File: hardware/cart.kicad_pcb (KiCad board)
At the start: 2 copper layers, 83.8 x 38.3 mm, 4 parts, among them P1 MD-CART-FINGERS

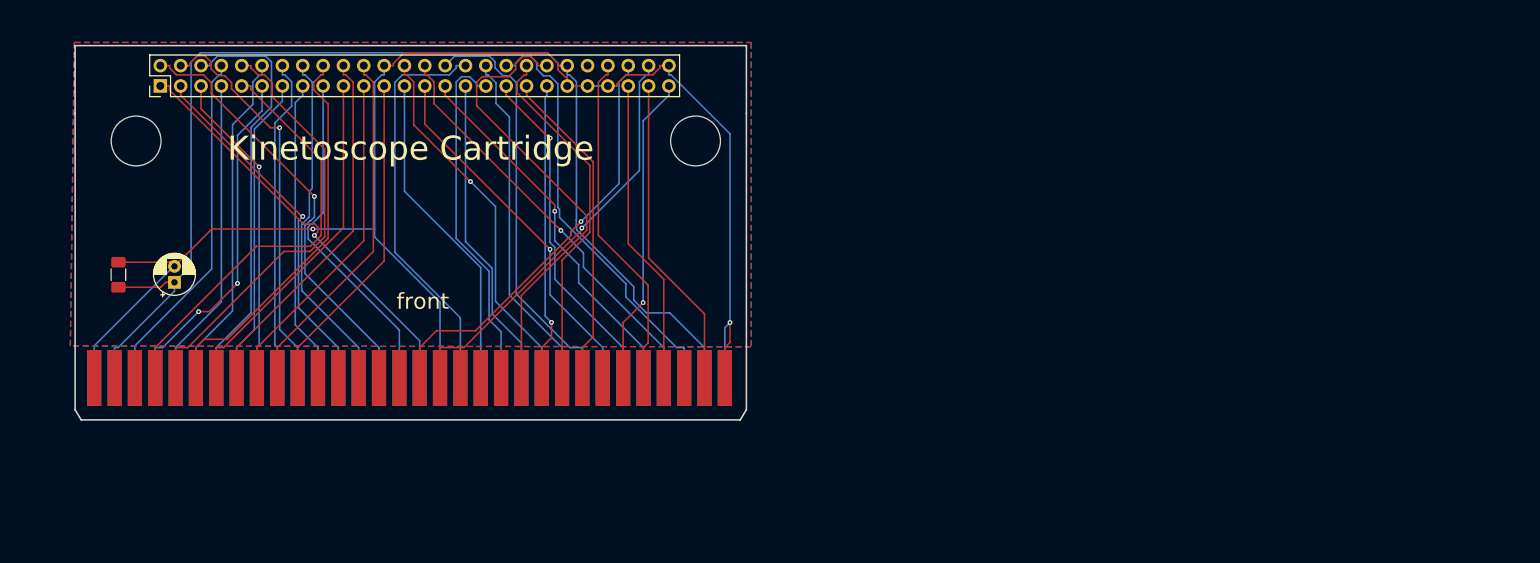
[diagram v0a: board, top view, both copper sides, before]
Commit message: Massively reorganize board designs
Now planning to have most assembly done by JLCPCB, so trace sizes,
part selections, etc. are set accordingly.

New boards are:
 - cartridge interface & flash
 - microcontroller & registers
 - sram x2
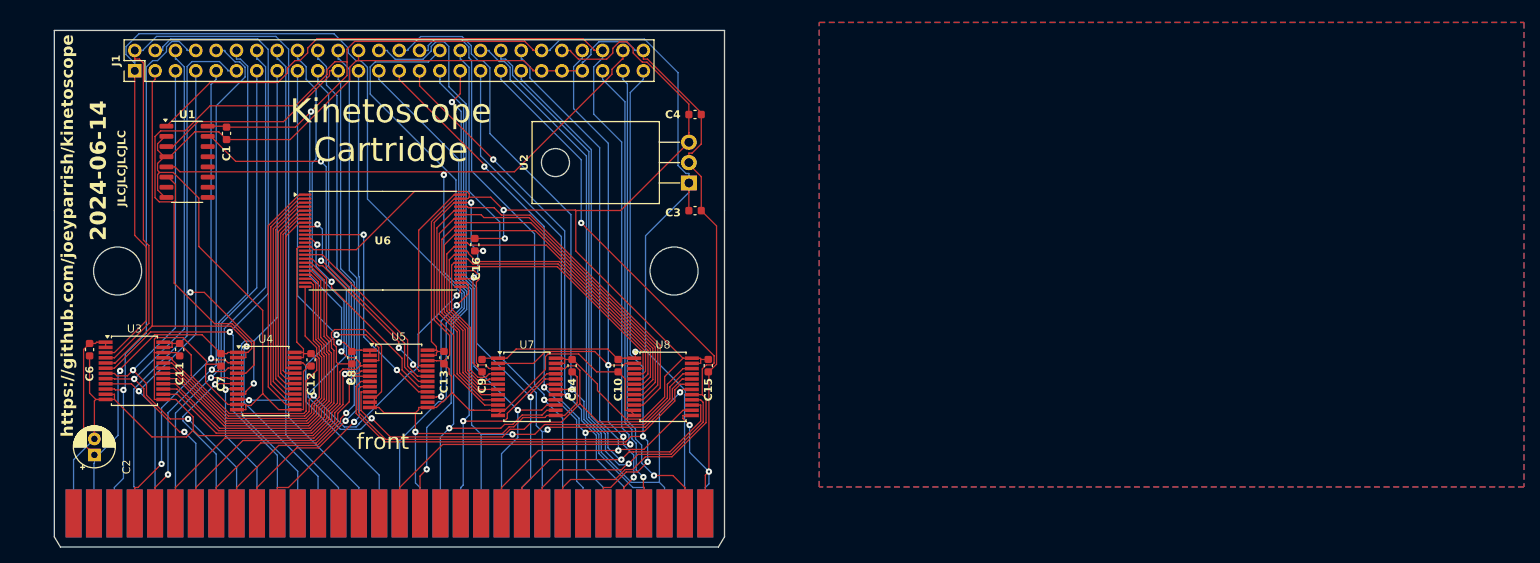
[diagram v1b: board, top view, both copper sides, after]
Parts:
- added C10: 22nF, Capacitor_SMD:C_0603_1608Metric, F.Cu at (83.4, 55.4)
- added C11: 22nF, Capacitor_SMD:C_0603_1608Metric, F.Cu at (28.6, 53.4)
- added C12: 22nF, Capacitor_SMD:C_0603_1608Metric, F.Cu at (45.0, 54.6)
- added C13: 22nF, Capacitor_SMD:C_0603_1608Metric, F.Cu at (61.6, 54.4)
- added C14: 22nF, Capacitor_SMD:C_0603_1608Metric, F.Cu at (77.7, 55.4)
- added C15: 22nF, Capacitor_SMD:C_0603_1608Metric, F.Cu at (94.7, 55.4)
- added C16: 22nF, Capacitor_SMD:C_0603_1608Metric, F.Cu at (65.5, 40.2)
- added C3: 4.7uF, Capacitor_SMD:C_0603_1608Metric, F.Cu at (93.0, 36.0)
- added C4: 1uF, Capacitor_SMD:C_0603_1608Metric, F.Cu at (93.0, 24.0)
- added C6: 22nF, Capacitor_SMD:C_0603_1608Metric, F.Cu at (17.4, 53.4)
- added C7: 22nF, Capacitor_SMD:C_0603_1608Metric, F.Cu at (33.8, 54.6)
- added C8: 22nF, Capacitor_SMD:C_0603_1608Metric, F.Cu at (50.1, 54.4)
- added C9: 22nF, Capacitor_SMD:C_0603_1608Metric, F.Cu at (66.4, 55.4)
- added U1: decoder, Package_SO:SO-16_3.9x9.9mm_P1.27mm, F.Cu at (29.6, 29.9)
- added U2: 1.5A @ 3.3V, Package_TO_SOT_THT:TO-220-3_Horizontal_TabDown, F.Cu at (92.2, 32.5)
- added U3: 3.3V <=> 5V, Package_SO:SSOP-24_5.3x8.2mm_P0.65mm, F.Cu at (23.0, 56.0)
- added U4: 3.3V <=> 5V, Package_SO:SSOP-24_5.3x8.2mm_P0.65mm, F.Cu at (39.4, 57.3)
- added U5: 3.3V <=> 5V, Package_SO:SSOP-24_5.3x8.2mm_P0.65mm, F.Cu at (56.0, 57.0)
- added U6: 1Mx16, Package_SO:TSOP-I-48_18.4x12mm_P0.5mm, F.Cu at (54.0, 39.8)
- added U7: 3.3V <=> 5V, Package_SO:SSOP-24_5.3x8.2mm_P0.65mm, F.Cu at (72.0, 58.0)
- added U8: 3.3V <=> 5V, Package_SO:SSOP-24_5.3x8.2mm_P0.65mm, F.Cu at (89.0, 58.0)
- C1: value 4.7uF -> 22nF; footprint Capacitor_THT:CP_Radial_D5.0mm_P2.00mm -> Capacitor_SMD:C_0603_1608Metric
- C2: value 22nF -> 47uF; footprint Capacitor_SMD:C_1206_3216Metric_Pad1.33x1.80mm_HandSolder -> Capacitor_THT:CP_Radial_D5.0mm_P2.00mm
- J1: footprint kinetoscope-cart-header:kinetoscope-cart-header-half -> Connector_PinHeader_2.54mm:PinHeader_2x26_P2.54mm_Vertical
- P1: value MD-CART-FINGERS -> edge connector
- moved P1 49.1 mm to (13.0, 78.0)
- moved C2 22.7 mm to (18.0, 66.5)
- moved C1 19.7 mm to (34.5, 26.4), turned to -90 degrees
- moved J1 3.72 mm to (23.0, 18.5)
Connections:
- net /5V renamed +5V
- net /GND renamed GND
- J1 pad 44: unconnected-(J1B-3V-Pad44) -> +3.3V
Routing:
- net GND: track 185.7 -> 475.9 mm, vias 2 -> 6
- net +3.3V: track 0.00 -> 222.9 mm, vias 0 -> 2
- net +5V: track 147.2 -> 314.1 mm, vias 0 -> 4
- net /~{FLASH_CE}: track 0.00 -> 118.4 mm, vias 0 -> 2
- net /~{SEGA_CE}: track 52.8 -> 146.2 mm
- net /SEGA_A1: track 51.7 -> 139.1 mm, vias 1 -> 0
- net /~{SEGA_WE_LB}: track 42.5 -> 119.4 mm, vias 0 -> 3
- net /SEGA_A2: track 54.0 -> 124.6 mm, vias 1 -> 0
- net /~{SEGA_RESET}: track 38.8 -> 103.4 mm, vias 1 -> 2
- net /~{SEGA_AS}: track 51.7 -> 110.5 mm, vias 1 -> 2
- net /flash-internal/A0_3V: track 0.00 -> 53.9 mm, vias 0 -> 2
- net /SEGA_A21: track 42.0 -> 90.7 mm, vias 0 -> 1
- net /SEGA_D14: track 37.4 -> 85.9 mm
- net /SEGA_A4: track 49.9 -> 95.3 mm
- net /SEGA_D13: track 44.8 -> 90.2 mm, vias 0 -> 1
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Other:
- board size 83.8 x 38.3 mm -> 83.7 x 42 mm
- board text added: "2024-06-14"
- board text added: "JLCJLCJLCJLC"
- board text added: "This edge beveled, hard-gold plating on these teeth, both sides"
- board text added: "https://github.com/joeyparrish/kinetoscope"
- board text removed: "back"
- board text removed: "front"

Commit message: Redo cart board
The first cartridge board I ordered did not work.  💰🚽

Problems I ran into:
 - The FlashKit Programmer sends 3.3V logic, not 5V logic like the
   Sega
 - I had one hard-coded input to my address decoder inverted
 - One pair of level translators had their supply voltages backward
 - I had hard-coded #OE on the flash chip, but #OE and #WE are
   mutually exclusive on this particular chip

Changes:
 - Add debug connectors (not populated by default) for power and flash
   control signals
 - Fix flash ~OE signal, which is mutually exclusive with ~WE
 - Fix level translators for compatibility with both 3.3V and 5V logic
 - Replace decoder with a smaller, simpler one with no latches and
   5V-tolerance
 - Reorient translators to simplify traces
 - Increase trace width for supply traces
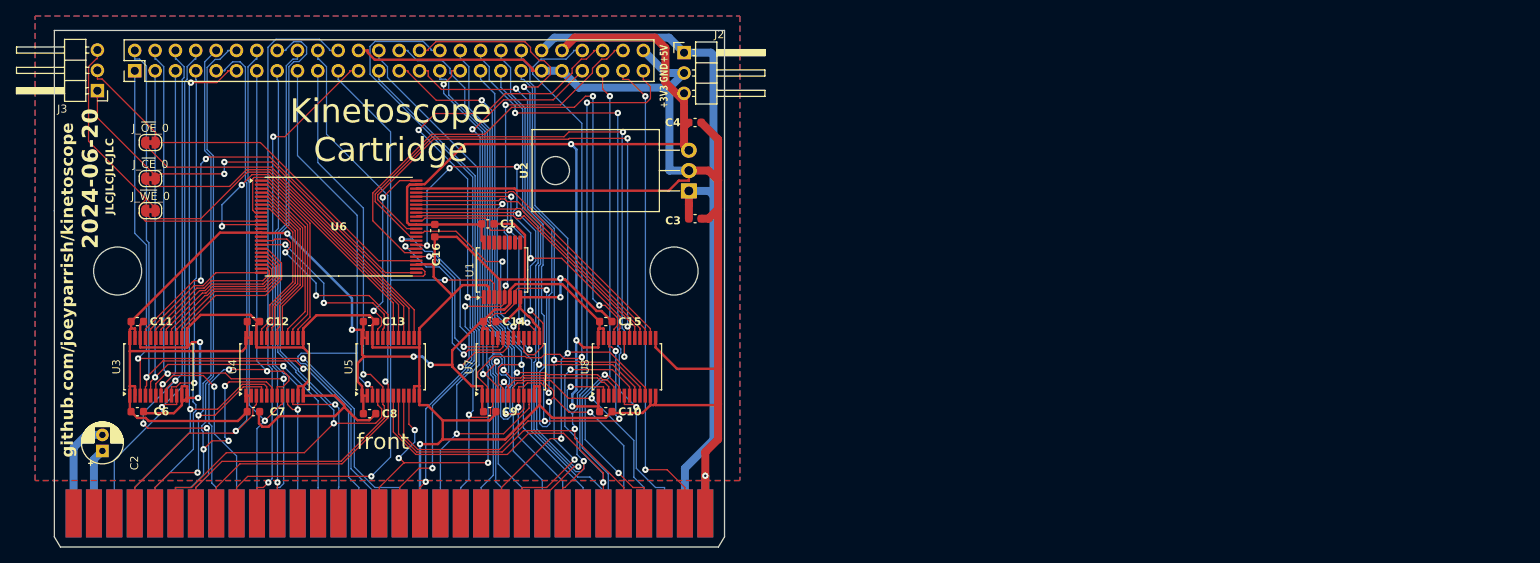
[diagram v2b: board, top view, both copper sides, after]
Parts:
- added J2: debug-power, Connector_PinHeader_2.54mm:PinHeader_1x03_P2.54mm_Horizontal, F.Cu at (91.6, 16.3)
- added J3: debug-flash, Connector_PinHeader_2.54mm:PinHeader_1x03_P2.54mm_Horizontal, F.Cu at (18.4, 21.0)
- added J_~{CE}_0: jumper-bridged, Jumper:SolderJumper-2_P1.3mm_Bridged_RoundedPad1.0x1.5mm, F.Cu at (25.0, 32.0)
- added J_~{OE}_0: jumper-bridged, Jumper:SolderJumper-2_P1.3mm_Bridged_RoundedPad1.0x1.5mm, F.Cu at (25.0, 27.5)
- added J_~{WE}_0: jumper-bridged, Jumper:SolderJumper-2_P1.3mm_Bridged_RoundedPad1.0x1.5mm, F.Cu at (25.0, 36.0)
- U1: value decoder -> 74LVC138; footprint Package_SO:SO-16_3.9x9.9mm_P1.27mm -> Package_SO:SSOP-16_5.3x6.2mm_P0.65mm
- U3, U4, U5, U7, U8: value 3.3V <=> 5V -> 74LVC8T245
- U6: value 1Mx16 -> S29AL016J55TFIR20
- moved U1 41.6 mm to (68.9, 43.4), turned to 90 degrees
- moved C1 34.5 mm to (67.1, 37.6), turned to 0 degrees
- moved C15 13.9 mm to (81.9, 49.9), turned to 0 degrees
- moved C14 11.7 mm to (67.4, 49.9), turned to 0 degrees
- moved C13 10.3 mm to (52.4, 49.9), turned to 0 degrees
- moved C6 9.77 mm to (23.4, 61.1), turned to 0 degrees
- moved C12 8.64 mm to (37.9, 49.9), turned to 0 degrees
- moved C7 7.63 mm to (37.9, 61.1), turned to 0 degrees
- moved C8 7.33 mm to (52.4, 61.4), turned to 0 degrees
- moved C11 6.35 mm to (23.4, 49.9), turned to 0 degrees
- moved C10 5.95 mm to (81.9, 61.1), turned to 0 degrees
- moved C9 5.82 mm to (67.4, 61.1), turned to 0 degrees
- moved U6 5.77 mm to (48.5, 38.0)
- moved C16 5.30 mm to (60.5, 38.5)
- moved U8 5.15 mm to (84.5, 55.5), turned to 90 degrees
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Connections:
- C1 pad 1: +5V -> +3.3V
- C10 pad 1: +5V -> +3.3V
- C2 pad 1: +5V -> +5VP
- C2 pad 2: GND -> GNDPWR
- C6 pad 1: +5V -> +3.3V
- C7 pad 1: +5V -> +3.3V
- C8 pad 1: +5V -> +3.3V
- C9 pad 1: +5V -> +3.3V
- J1 pad 45: GND -> /~{SEGA_OE}
- P1 pad A1: GND -> GNDPWR
- P1 pad A2: +5V -> +5VP
- P1 pad B16: unconnected-(P1-~{C_OE}-PadB16) -> /~{SEGA_OE}
- U1 pad 15: /~{FLASH_CE} -> unconnected-(U1-~{Y0}-Pad15)
- U1 pad 16: +5V -> +3.3V
- U1 pad 6: +5V -> +3.3V
- U1 pad 7: unconnected-(U1-Y7-Pad7) -> /~{FLASH_CE}
- U3 pad 1: +5V -> +3.3V
- U3 pad 2: +5V -> +3.3V
- U4 pad 1: +5V -> +3.3V
- U4 pad 2: +5V -> +3.3V
- U5 pad 1: +5V -> +3.3V
- U5 pad 10: GND -> /~{SEGA_OE}
- U5 pad 14: unconnected-(U5-B8-Pad14) -> Net-(J_~{OE}_0-A)
- U5 pad 15: /flash-internal/~{CE_3V} -> Net-(J_~{CE}_0-A)
- U5 pad 16: /flash-internal/~{WE_3V} -> Net-(J_~{WE}_0-A)
- U5 pad 2: +5V -> +3.3V
- U6 pad 28: GND -> /flash-internal/~{OE_3V}
- U7 pad 1: +5V -> +3.3V
- U7 pad 10: /flash-internal/D7_3V -> /SEGA_D7
- U7 pad 14: /SEGA_D7 -> /flash-internal/D7_3V
- U7 pad 15: /SEGA_D6 -> /flash-internal/D6_3V
- U7 pad 16: /SEGA_D5 -> /flash-internal/D5_3V
- U7 pad 17: /SEGA_D4 -> /flash-internal/D4_3V
- U7 pad 18: /SEGA_D3 -> /flash-internal/D3_3V
- U7 pad 19: /SEGA_D2 -> /flash-internal/D2_3V
- U7 pad 20: /SEGA_D1 -> /flash-internal/D1_3V
- U7 pad 21: /SEGA_D0 -> /flash-internal/D0_3V
- U7 pad 3: /flash-internal/D0_3V -> /SEGA_D0
- U7 pad 4: /flash-internal/D1_3V -> /SEGA_D1
- U7 pad 5: /flash-internal/D2_3V -> /SEGA_D2
- U7 pad 6: /flash-internal/D3_3V -> /SEGA_D3
- U7 pad 7: /flash-internal/D4_3V -> /SEGA_D4
- U7 pad 8: /flash-internal/D5_3V -> /SEGA_D5
- U7 pad 9: /flash-internal/D6_3V -> /SEGA_D6
- U8 pad 1: +5V -> +3.3V
- U8 pad 10: /flash-internal/D15_3V -> /SEGA_D15
- U8 pad 14: /SEGA_D15 -> /flash-internal/D15_3V
- U8 pad 15: /SEGA_D14 -> /flash-internal/D14_3V
- U8 pad 16: /SEGA_D13 -> /flash-internal/D13_3V
- U8 pad 17: /SEGA_D12 -> /flash-internal/D12_3V
- U8 pad 18: /SEGA_D11 -> /flash-internal/D11_3V
- U8 pad 19: /SEGA_D10 -> /flash-internal/D10_3V
- U8 pad 20: /SEGA_D9 -> /flash-internal/D9_3V
- U8 pad 21: /SEGA_D8 -> /flash-internal/D8_3V
- U8 pad 3: /flash-internal/D8_3V -> /SEGA_D8
- U8 pad 4: /flash-internal/D9_3V -> /SEGA_D9
- U8 pad 5: /flash-internal/D10_3V -> /SEGA_D10
- U8 pad 6: /flash-internal/D11_3V -> /SEGA_D11
- U8 pad 7: /flash-internal/D12_3V -> /SEGA_D12
- U8 pad 8: /flash-internal/D13_3V -> /SEGA_D13
- U8 pad 9: /flash-internal/D14_3V -> /SEGA_D14
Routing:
- net +5V: track 314.1 -> 90.2 mm, vias 4 -> 0
- net /~{SEGA_OE}: track 0.00 -> 87.1 mm, vias 0 -> 4
- net +3.3V: track 222.9 -> 286.8 mm, vias 2 -> 7
- net /~{SEGA_CE}: track 146.2 -> 85.1 mm, vias 1 -> 3
- net /flash-internal/~{OE_3V}: track 0.00 -> 51.0 mm
- net /SEGA_A1: track 139.1 -> 88.4 mm, vias 0 -> 2
- net Net-(J_~{WE}_0-A): track 0.00 -> 46.2 mm
- net Net-(J_~{OE}_0-A): track 0.00 -> 45.9 mm
- net Net-(J_~{CE}_0-A): track 0.00 -> 45.3 mm
- net /flash-internal/D8_3V: track 30.4 -> 75.1 mm, vias 0 -> 2
- net /~{FLASH_CE}: track 118.4 -> 73.8 mm, vias 2 -> 4
- net GND: track 475.9 -> 436.0 mm
- net /flash-internal/D10_3V: track 33.6 -> 72.6 mm, vias 0 -> 2
- net /flash-internal/~{CE_3V}: track 18.2 -> 56.9 mm
- net /SEGA_A2: track 124.6 -> 86.4 mm, vias 0 -> 2
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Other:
- board text added: "+3V3"
- board text added: "+5V"
- board text added: "2024-06-20"
- board text added: "GND"
- board text added: "github.com/joeyparrish/kinetoscope"
- board text removed: "2024-06-14"
- board text removed: "https://github.com/joeyparrish/kinetoscope"

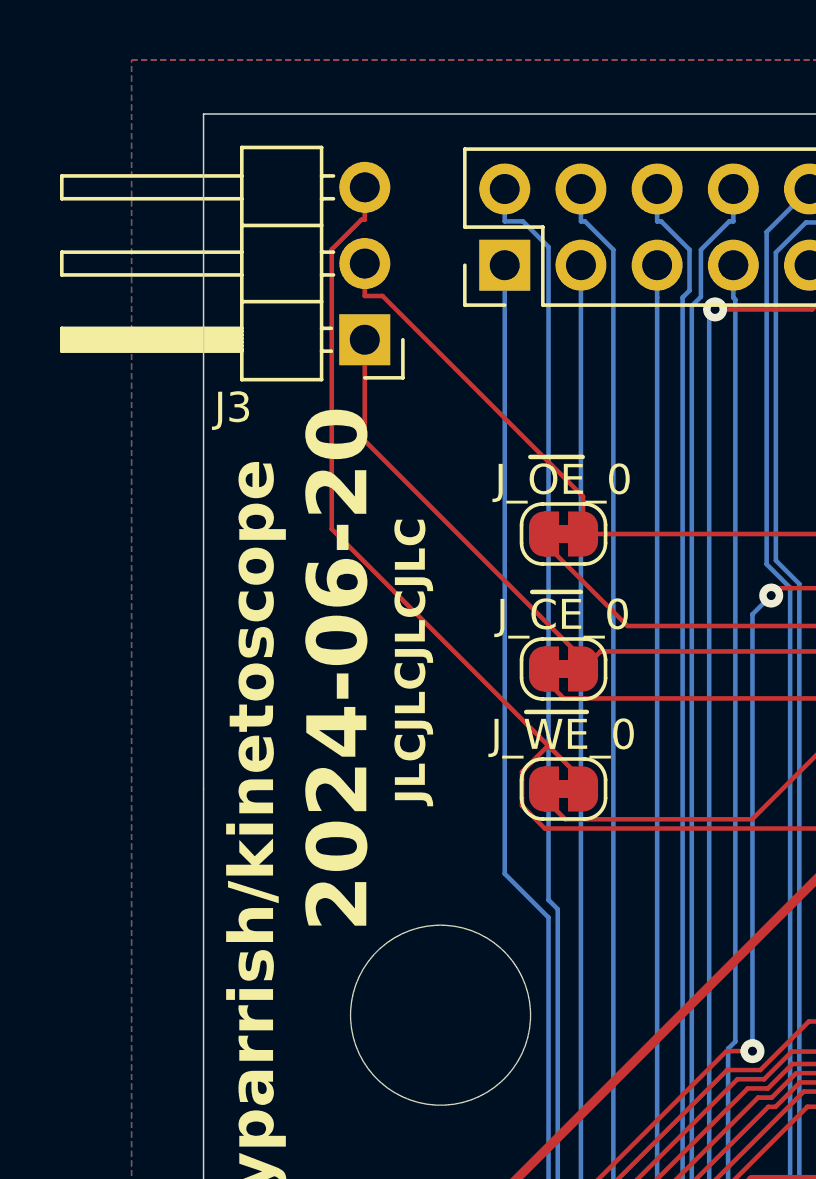
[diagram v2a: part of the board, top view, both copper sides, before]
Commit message: Add notes on JLCPCB orders, add labels to debug connector
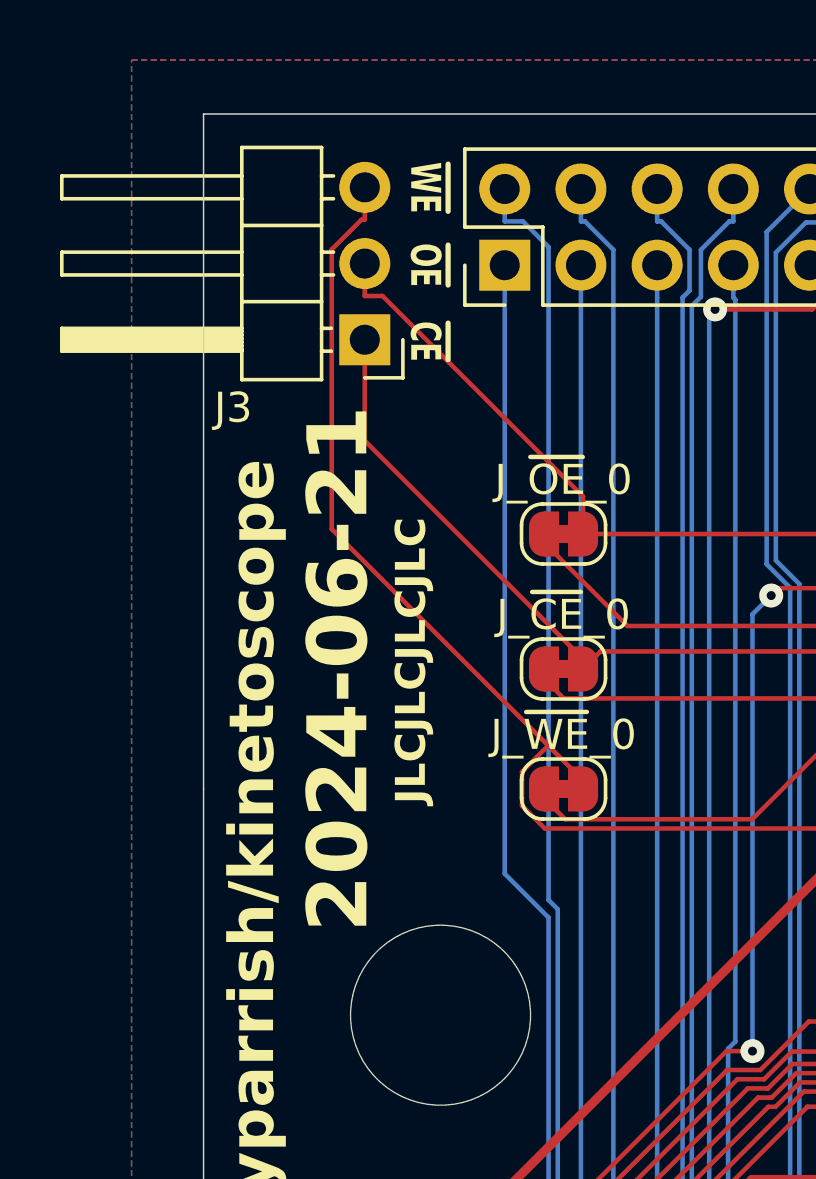
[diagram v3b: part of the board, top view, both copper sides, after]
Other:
- board text added: "2024-06-21"
- board text added: "~{CE}"
- board text added: "~{OE}"
- board text added: "~{WE}"
- board text removed: "2024-06-20"
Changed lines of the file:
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@@
+		)
+	)
+	(gr_text "~{CE}"
+		(at 19.8 20.4 270)
+		(layer "F.SilkS")
+		(effects
+			(font
+				(size 1 0.7)
+				(thickness 0.175)
+				(bold yes)
+			)
+			(justify left bottom)
 		)
 	)
@@
 		)
 	)
+	(gr_text "~{WE}"
+		(at 19.8 15.1 270)
+		(layer "F.SilkS")
+		(effects
+			(font
+				(size 1 0.7)
+				(thickness 0.175)
+				(bold yes)
+			)
+			(justify left bottom)
+		)
+	)
 	(gr_text "github.com/joeyparrish/kinetoscope"
 		(at 15.5 25 90)
@@
 		)
 	)
-	(gr_text "2024-06-20"
+	(gr_text "~{OE}"
+		(at 19.8 17.8 270)
+		(layer "F.SilkS")
+		(effects
+			(font
+				(size 1 0.7)
+				(thickness 0.175)
+				(bold yes)
+			)
+			(justify left bottom)
+		)
+	)
+	(gr_text "2024-06-21"
 		(at 17.5 32 90)
 		(layer "F.SilkS")
@@
 			)
 		)
-		(render_cache "2024-06-20" 90
+		(render_cache "2024-06-21" 90
 			(polygon
 				(pts
@@
 			(polygon
 				(pts
-					(xy 18.33 24.034263) (xy 18.33 24.844661) (xy 17.976336 25.08353) (xy 16.589036 25.08353) (xy 16.329162 24.844661)
-					(xy 16.329162 24.166643) (xy 16.573405 24.166643) (xy 16.573405 24.743056) (xy 16.667194 24.81926)
-					(xy 17.595317 24.81926) (xy 16.818625 24.067969) (xy 17.141025 24.067969) (xy 17.92016 24.81926)
-					(xy 17.940188 24.81926) (xy 18.085757 24.717655) (xy 18.085757 24.141241) (xy 18.00711 24.067969)
-					(xy 17.141025 24.067969) (xy 16.818625 24.067969) (xy 16.734117 24.067969) (xy 16.573405 24.166643)
-					(xy 16.329162 24.166643) (xy 16.329162 24.034263) (xy 16.692107 23.800767) (xy 18.082826 23.800767)
-				)
-			)
+					(xy 16.329162 24.563293) (xy 16.329162 24.307327) (xy 18.085757 24.307327) (xy 18.085757 23.800767)
+					(xy 18.33 23.800767) (xy 18.33 25.08353) (xy 18.085757 25.08353) (xy 18.085757 24.574528) (xy 16.703831 24.574528)
+					(xy 17.054075 24.912072) (xy 16.843538 25.049825)
+				)
+			)
